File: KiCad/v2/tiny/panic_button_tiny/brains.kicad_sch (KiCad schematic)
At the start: 1 part, among them U1 ESP32-C3

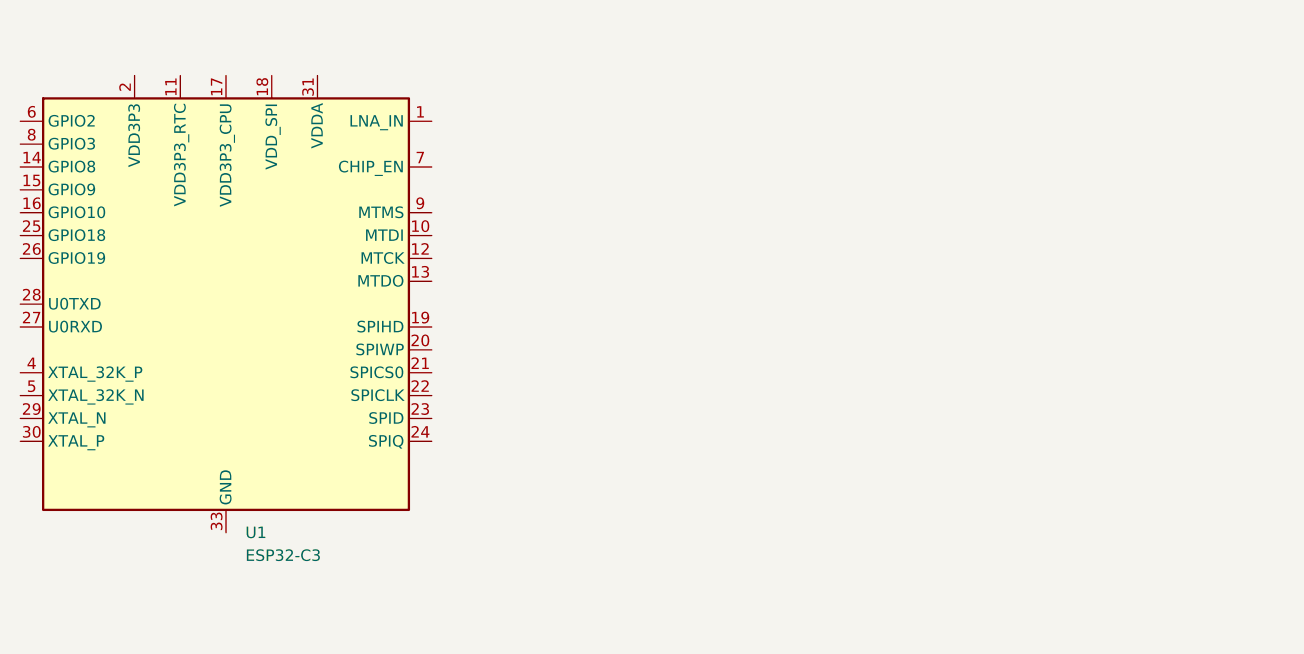
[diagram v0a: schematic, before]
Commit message: [UPDATE] the structure of the KiCad design for the tiny version
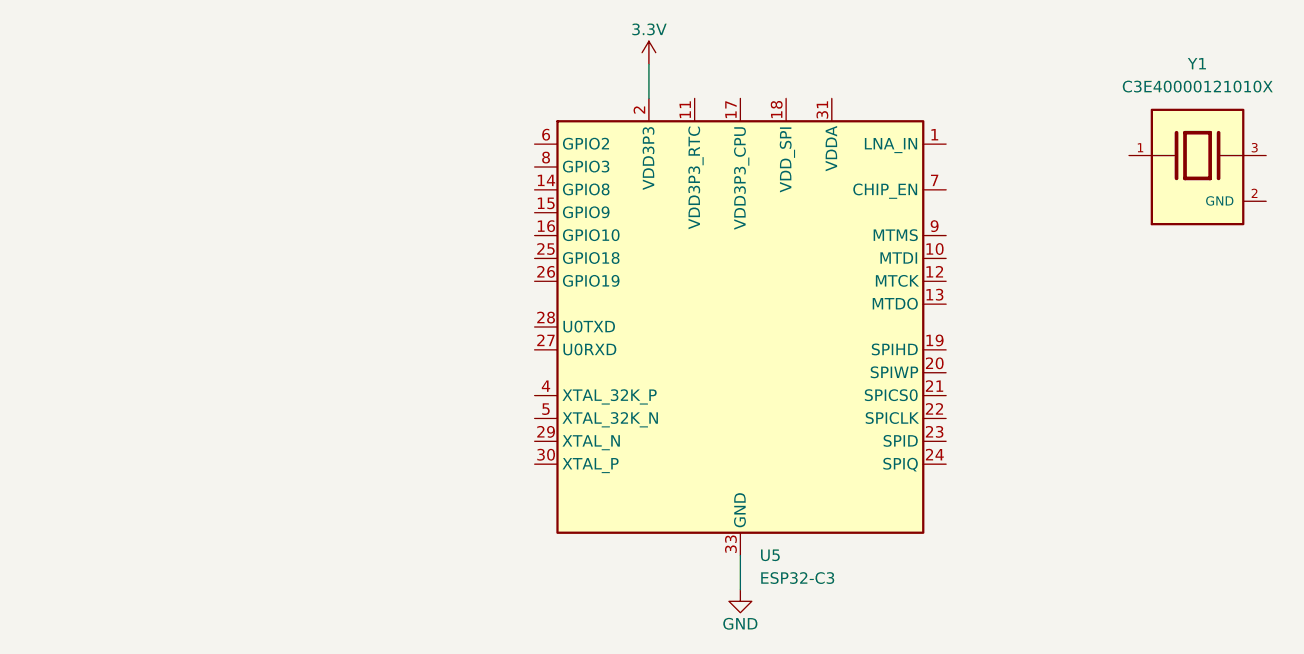
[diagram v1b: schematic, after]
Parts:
- added Y1: C3E40000121010X, C3E40000121010X:XTAL_C3E40000121010X, symbol C3E40000121010X:C3E40000121010X
- renumbered U1 to U5
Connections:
- net 3.3V: now reaches U5.2 (VDD3P3), U5.3 (VDD3P3)
- net GND: now reaches U5.33 (GND)
- net GND: now also Y1.2 (GND), Y1.4 (GND)
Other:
- moved on the sheet: U5

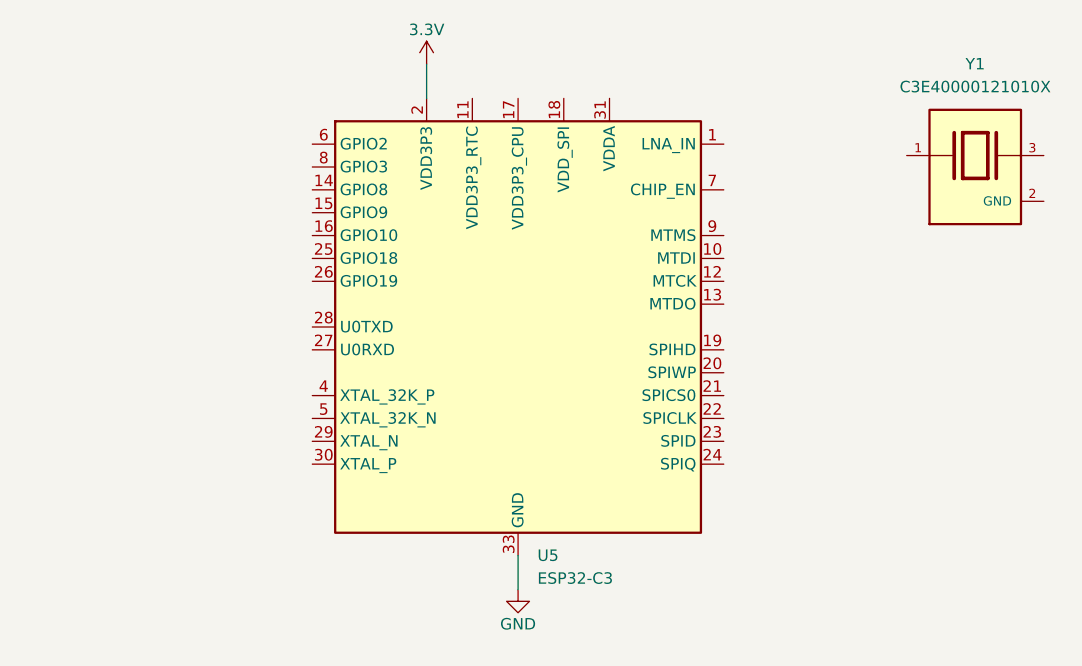
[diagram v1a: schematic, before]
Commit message: [UPDATE] the KiCad schematic to contain some of the updated designs for the circuit
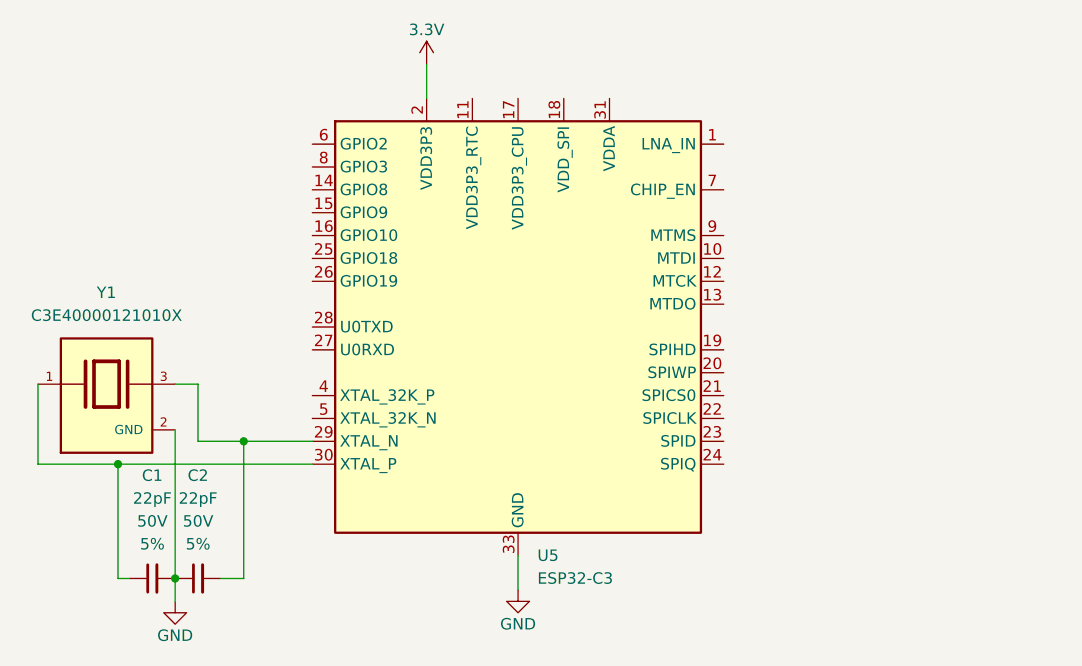
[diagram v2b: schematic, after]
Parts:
- added C1, C2: 22pF, PCM_SparkFun-Capacitor:C_0402_1005Metric, symbol PCM_SparkFun-Capacitor:22pF_0402_50V_5%
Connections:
- net GND: now also C1.2, C2.1
- net at Y1.1: now also U5.30 (XTAL_P), C1.1
- net at Y1.3: now also U5.29 (XTAL_N), C2.2
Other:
- moved on the sheet: Y1

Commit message: [UPDATE] the schematic to reflect the connections of the components
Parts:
- renumbered C1 to C2, C2 to C3
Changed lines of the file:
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@@
 		(dnp no)
 		(fields_autoplaced yes)
-		(property "Reference" "C2"
+		(property "Reference" "C3"
 			(at 67.3163 64.77 90)
 			(show_name no)
@@
 			(project "panic_button_tiny"
 				(path "/c4eb92e9-b42f-4db0-b1d9-0ef70f7ca601/525ab16f-d6f3-4728-a011-f4f1ced9fd5e"
-					(reference "C2")
+					(reference "C3")
 					(unit 1)
 				)
@@
 		(dnp no)
 		(fields_autoplaced yes)
-		(property "Reference" "C1"
+		(property "Reference" "C2"
 			(at 62.2363 64.77 90)
 			(show_name no)
@@
 			(project "panic_button_tiny"
 				(path "/c4eb92e9-b42f-4db0-b1d9-0ef70f7ca601/525ab16f-d6f3-4728-a011-f4f1ced9fd5e"
-					(reference "C1")
+					(reference "C2")
 					(unit 1)
 				)
@@
 		(dnp no)
 		(fields_autoplaced yes)
-		(property "Reference" "#PWR08"
+		(property "Reference" "#PWR050"
 			(at 102.87 83.82 0)
 			(hide yes)
@@
 			(project "panic_button_tiny"
 				(path "/c4eb92e9-b42f-4db0-b1d9-0ef70f7ca601/525ab16f-d6f3-4728-a011-f4f1ced9fd5e"
-					(reference "#PWR08")
+					(reference "#PWR050")
 					(unit 1)
 				)
@@
 		(dnp no)
 		(fields_autoplaced yes)
-		(property "Reference" "#PWR06"
+		(property "Reference" "#PWR048"
 			(at 64.77 85.09 0)
 			(hide yes)
@@
 			(project "panic_button_tiny"
 				(path "/c4eb92e9-b42f-4db0-b1d9-0ef70f7ca601/525ab16f-d6f3-4728-a011-f4f1ced9fd5e"
-					(reference "#PWR06")
+					(reference "#PWR048")
 					(unit 1)
 				)
@@
 		(dnp no)
 		(fields_autoplaced yes)
-		(property "Reference" "#PWR07"
+		(property "Reference" "#PWR049"
 			(at 92.71 22.86 0)
 			(hide yes)
@@
 			(project "panic_button_tiny"
 				(path "/c4eb92e9-b42f-4db0-b1d9-0ef70f7ca601/525ab16f-d6f3-4728-a011-f4f1ced9fd5e"
-					(reference "#PWR07")
+					(reference "#PWR049")
 					(unit 1)
 				)

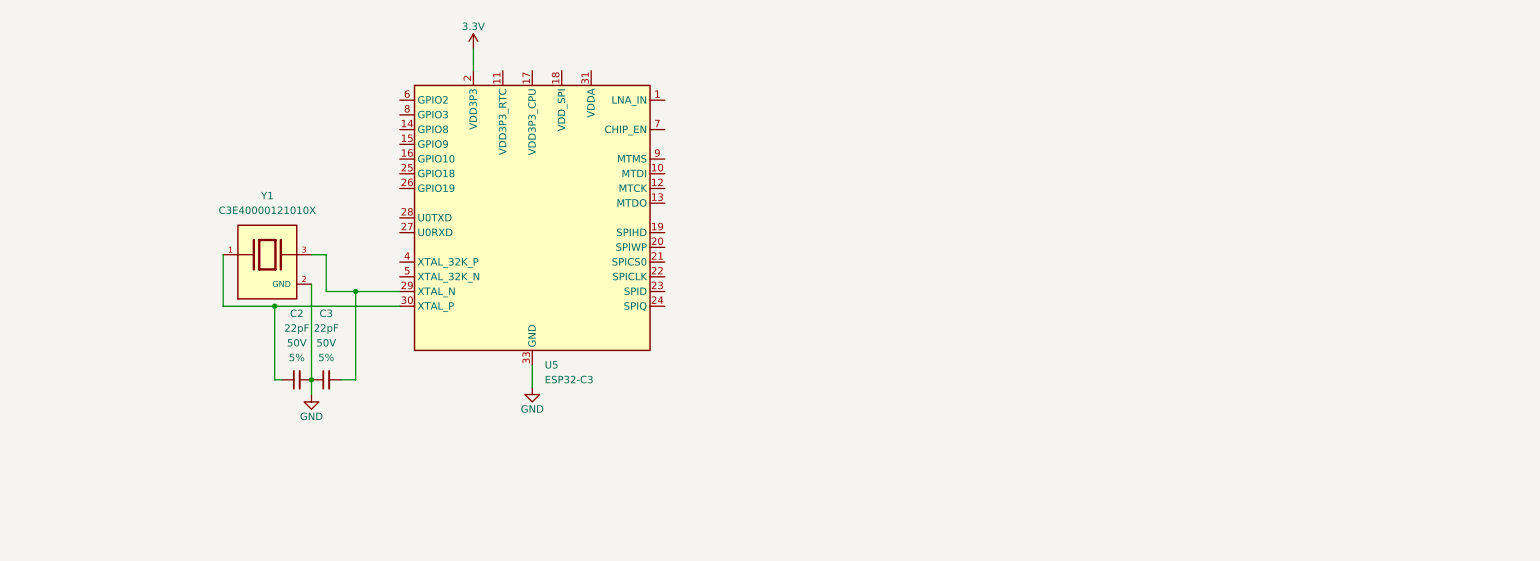
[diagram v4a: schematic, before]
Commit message: [UPDATE] the schematic with a buzzer and wirering for the different components
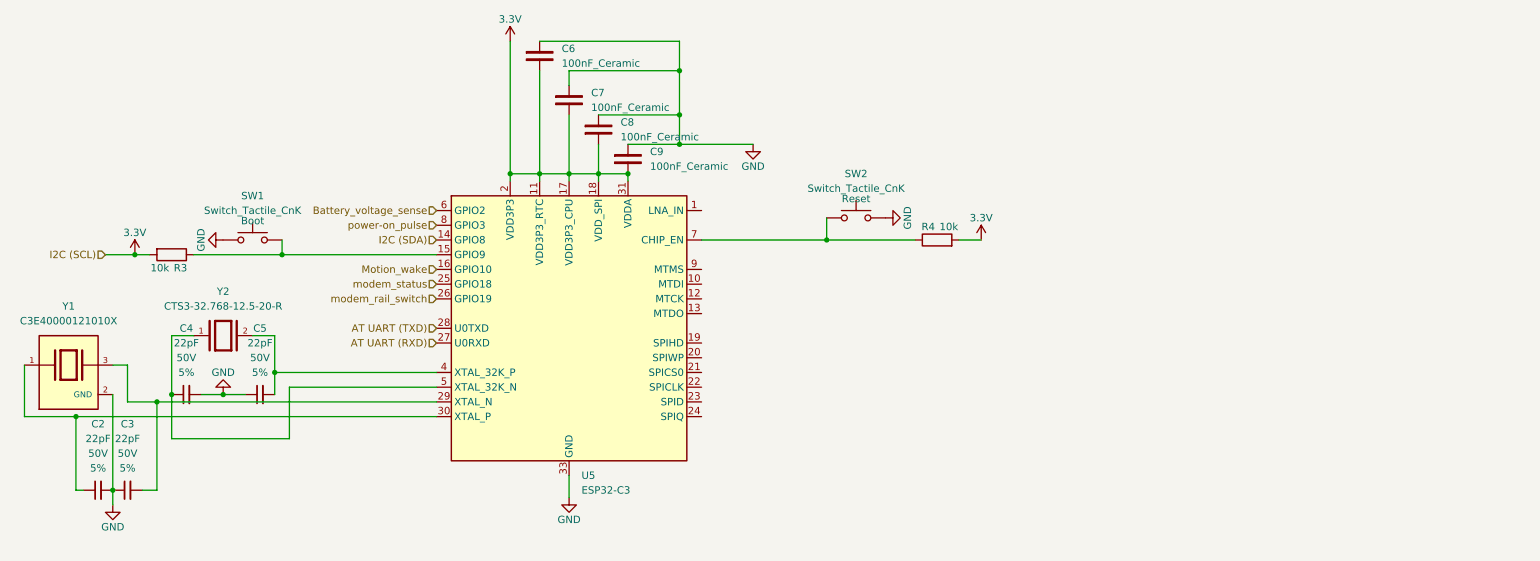
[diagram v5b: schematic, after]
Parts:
- added C4, C5: 22pF, PCM_SparkFun-Capacitor:C_0402_1005Metric, symbol PCM_SparkFun-Capacitor:22pF_0402_50V_5%
- added C6, C7, C8, C9: 100nF_Ceramic, Capacitor_THT:C_Disc_D5.0mm_W2.5mm_P2.50mm, symbol PCM_SL_Capacitors:100nF_Ceramic
- added R3, R4: 10k_0402, Resistor_SMD:R_0402_1005Metric, symbol PCM_4ms_Resistor:10k_0402
- added SW1, SW2: Switch_Tactile_CnK, PCM_fab:Button_CnK_PTS636.0_6x3.5mm, symbol PCM_fab:Switch_Tactile_CnK
- added Y2: CTS3-32.768-12.5-20-R, CTS3-32.768-12.5-20-R:XTAL_CTS3-32.768-12.5-20-R, symbol CTS3-32.768-12.5-20-R:CTS3-32.768-12.5-20-R
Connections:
- net 3.3V: now also U5.11 (VDD3P3_RTC), U5.17 (VDD3P3_CPU), U5.18 (VDD_SPI), U5.31 (VDDA), U5.32 (VDDA), C6.1, C7.1, C8.1, C9.1, R3.2, R4.2
- net GND: now also C4.2, C5.1, C6.2, C7.2, C8.2, C9.2, SW1.1, SW2.2
- net I2C (SDA): now reaches U5.14 (GPIO8)
- net at U5.15 (GPIO9): now also R3.1, SW1.2
- net Motion_wake: now reaches U5.16 (GPIO10)
- net modem_status: now reaches U5.25 (GPIO18)
- net modem_rail_switch: now reaches U5.26 (GPIO19)
- net AT UART (RXD): now reaches U5.27 (U0RXD)
- net AT UART (TXD): now reaches U5.28 (U0TXD)
- net at U5.4 (XTAL_32K_P): now also C5.2, Y2.2
- net at U5.5 (XTAL_32K_N): now also C4.1, Y2.1
- net Battery_voltage_sense: now reaches U5.6 (GPIO2)
- net at U5.7 (CHIP_EN): now also R4.1, SW2.1
- net power-on_pulse: now reaches U5.8 (GPIO3)
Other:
- moved on the sheet: C2, C3, U5, Y1

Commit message: [UPDATE] the schematic to contain more connections for the battery section
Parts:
- added SW3: Switch_Tactile_CnK, PCM_fab:Button_CnK_PTS636.0_6x3.5mm, symbol PCM_fab:Switch_Tactile_CnK
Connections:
- net GND: now also SW3.2
- net Motion_wake: now also U5.10 (MTDI); no longer U5.16 (GPIO10)
- net at U5.9 (MTMS): now also SW3.1
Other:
- note added: "(GPIO4)"
- note added: "(GPIO5)"
- note added: "(GPIO6)"
- note added: "(GPIO7)"
- moved on the sheet: SW2

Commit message: [UPDATED] annotations
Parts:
- renumbered C6 to C10, C7 to C11, C8 to C12, C9 to C13, C2 to C6, C3 to C7, C4 to C8, C5 to C9
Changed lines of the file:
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@@
 		(dnp no)
 		(fields_autoplaced yes)
-		(property "Reference" "C3"
+		(property "Reference" "C7"
 			(at 33.0263 83.82 90)
 			(show_name no)
@@
 			(project "panic_button_tiny"
 				(path "/c4eb92e9-b42f-4db0-b1d9-0ef70f7ca601/525ab16f-d6f3-4728-a011-f4f1ced9fd5e"
-					(reference "C3")
+					(reference "C7")
 					(unit 1)
 				)
@@
 		(dnp no)
 		(fields_autoplaced yes)
-		(property "Reference" "C9"
+		(property "Reference" "C13"
 			(at 123.19 36.8299 90)
 			(show_name no)
@@
 			(project "panic_button_tiny"
 				(path "/c4eb92e9-b42f-4db0-b1d9-0ef70f7ca601/525ab16f-d6f3-4728-a011-f4f1ced9fd5e"
-					(reference "C9")
+					(reference "C13")
 					(unit 1)
 				)
@@
 		(dnp no)
 		(fields_autoplaced yes)
-		(property "Reference" "C2"
+		(property "Reference" "C6"
 			(at 27.9463 83.82 90)
 			(show_name no)
@@
 			(project "panic_button_tiny"
 				(path "/c4eb92e9-b42f-4db0-b1d9-0ef70f7ca601/525ab16f-d6f3-4728-a011-f4f1ced9fd5e"
-					(reference "C2")
+					(reference "C6")
 					(unit 1)
 				)
@@
 		(dnp no)
 		(fields_autoplaced yes)
-		(property "Reference" "C6"
+		(property "Reference" "C10"
 			(at 107.95 19.0499 90)
 			(show_name no)
@@
 			(project "panic_button_tiny"
 				(path "/c4eb92e9-b42f-4db0-b1d9-0ef70f7ca601/525ab16f-d6f3-4728-a011-f4f1ced9fd5e"
-					(reference "C6")
+					(reference "C10")
 					(unit 1)
 				)
@@
 		(dnp no)
 		(fields_autoplaced yes)
-		(property "Reference" "C5"
+		(property "Reference" "C9"
 			(at 55.8863 67.31 90)
 			(show_name no)
@@
 			(project "panic_button_tiny"
 				(path "/c4eb92e9-b42f-4db0-b1d9-0ef70f7ca601/525ab16f-d6f3-4728-a011-f4f1ced9fd5e"
-					(reference "C5")
+					(reference "C9")
 					(unit 1)
 				)
@@
 		(dnp no)
 		(fields_autoplaced yes)
-		(property "Reference" "C7"
+		(property "Reference" "C11"
 			(at 113.03 26.6699 90)
 			(show_name no)
@@
 			(project "panic_button_tiny"
 				(path "/c4eb92e9-b42f-4db0-b1d9-0ef70f7ca601/525ab16f-d6f3-4728-a011-f4f1ced9fd5e"
-					(reference "C7")
+					(reference "C11")
 					(unit 1)
 				)
@@
 		(dnp no)
 		(fields_autoplaced yes)
-		(property "Reference" "C8"
+		(property "Reference" "C12"
 			(at 118.11 31.7499 90)
 			(show_name no)
@@
 			(project "panic_button_tiny"
 				(path "/c4eb92e9-b42f-4db0-b1d9-0ef70f7ca601/525ab16f-d6f3-4728-a011-f4f1ced9fd5e"
-					(reference "C8")
+					(reference "C12")
 					(unit 1)
 				)
@@
 		(dnp no)
 		(fields_autoplaced yes)
-		(property "Reference" "C4"
+		(property "Reference" "C8"
 			(at 43.1863 67.31 90)
 			(show_name no)
@@
 			(project "panic_button_tiny"
 				(path "/c4eb92e9-b42f-4db0-b1d9-0ef70f7ca601/525ab16f-d6f3-4728-a011-f4f1ced9fd5e"
-					(reference "C4")
+					(reference "C8")
 					(unit 1)
 				)

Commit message: [UPDATE] some connections in the schematic
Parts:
- added J3: PINHD_1x6_Male, Connector_PinHeader_2.54mm:PinHeader_1x06_P2.54mm_Vertical, symbol PCM_SL_Pin_Headers:PINHD_1x6_Male
- added R4: 4.7k_0603, PCM_4ms_Resistor:R_0603, symbol PCM_4ms_Resistor:4.7k_0603
- added TP1: 3.3V, TestPoint:TestPoint_Pad_D4.0mm, symbol Connector:TestPoint
- added TP2: U0TXD, TestPoint:TestPoint_Pad_D4.0mm, symbol Connector:TestPoint
- added TP3: CHIP_EN, TestPoint:TestPoint_Pad_D4.0mm, symbol Connector:TestPoint
- added TP4: GND, TestPoint:TestPoint_Pad_D4.0mm, symbol Connector:TestPoint
- added TP5: U0RXD, TestPoint:TestPoint_Pad_D4.0mm, symbol Connector:TestPoint
- added TP6: GPIO9, TestPoint:TestPoint_Pad_D4.0mm, symbol Connector:TestPoint
- renumbered R4 to R5
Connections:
- net 3.3V: now also J3.1, R4.1, TP1.1
- net GND: now also J3.2, TP4.1
- net I2C (SDA): now also R4.2
- net I2C (SCL): now reaches R3.1, SW1.2, U5.15 (GPIO9)
- net I2C (SCL): now also J3.6, TP6.1
- net at R5.1, SW2.1, U5.7 (CHIP_EN): now also J3.5, TP3.1
- net LED DIN: now reaches U5.16 (GPIO10)
- net AT UART (RXD) renamed UART (RXD)
- net UART (RXD): now also J3.4, TP5.1
- net AT UART (TXD) renamed UART (TXD)
- net UART (TXD): now also J3.3, TP2.1
- net Battery_voltage_sense renamed battery_voltage_sense
